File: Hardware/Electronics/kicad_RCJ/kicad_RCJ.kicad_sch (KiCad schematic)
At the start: 46 parts, among them J1 Raspberry_Pi_2_3, U23 TCS34725, U24 APDS9960

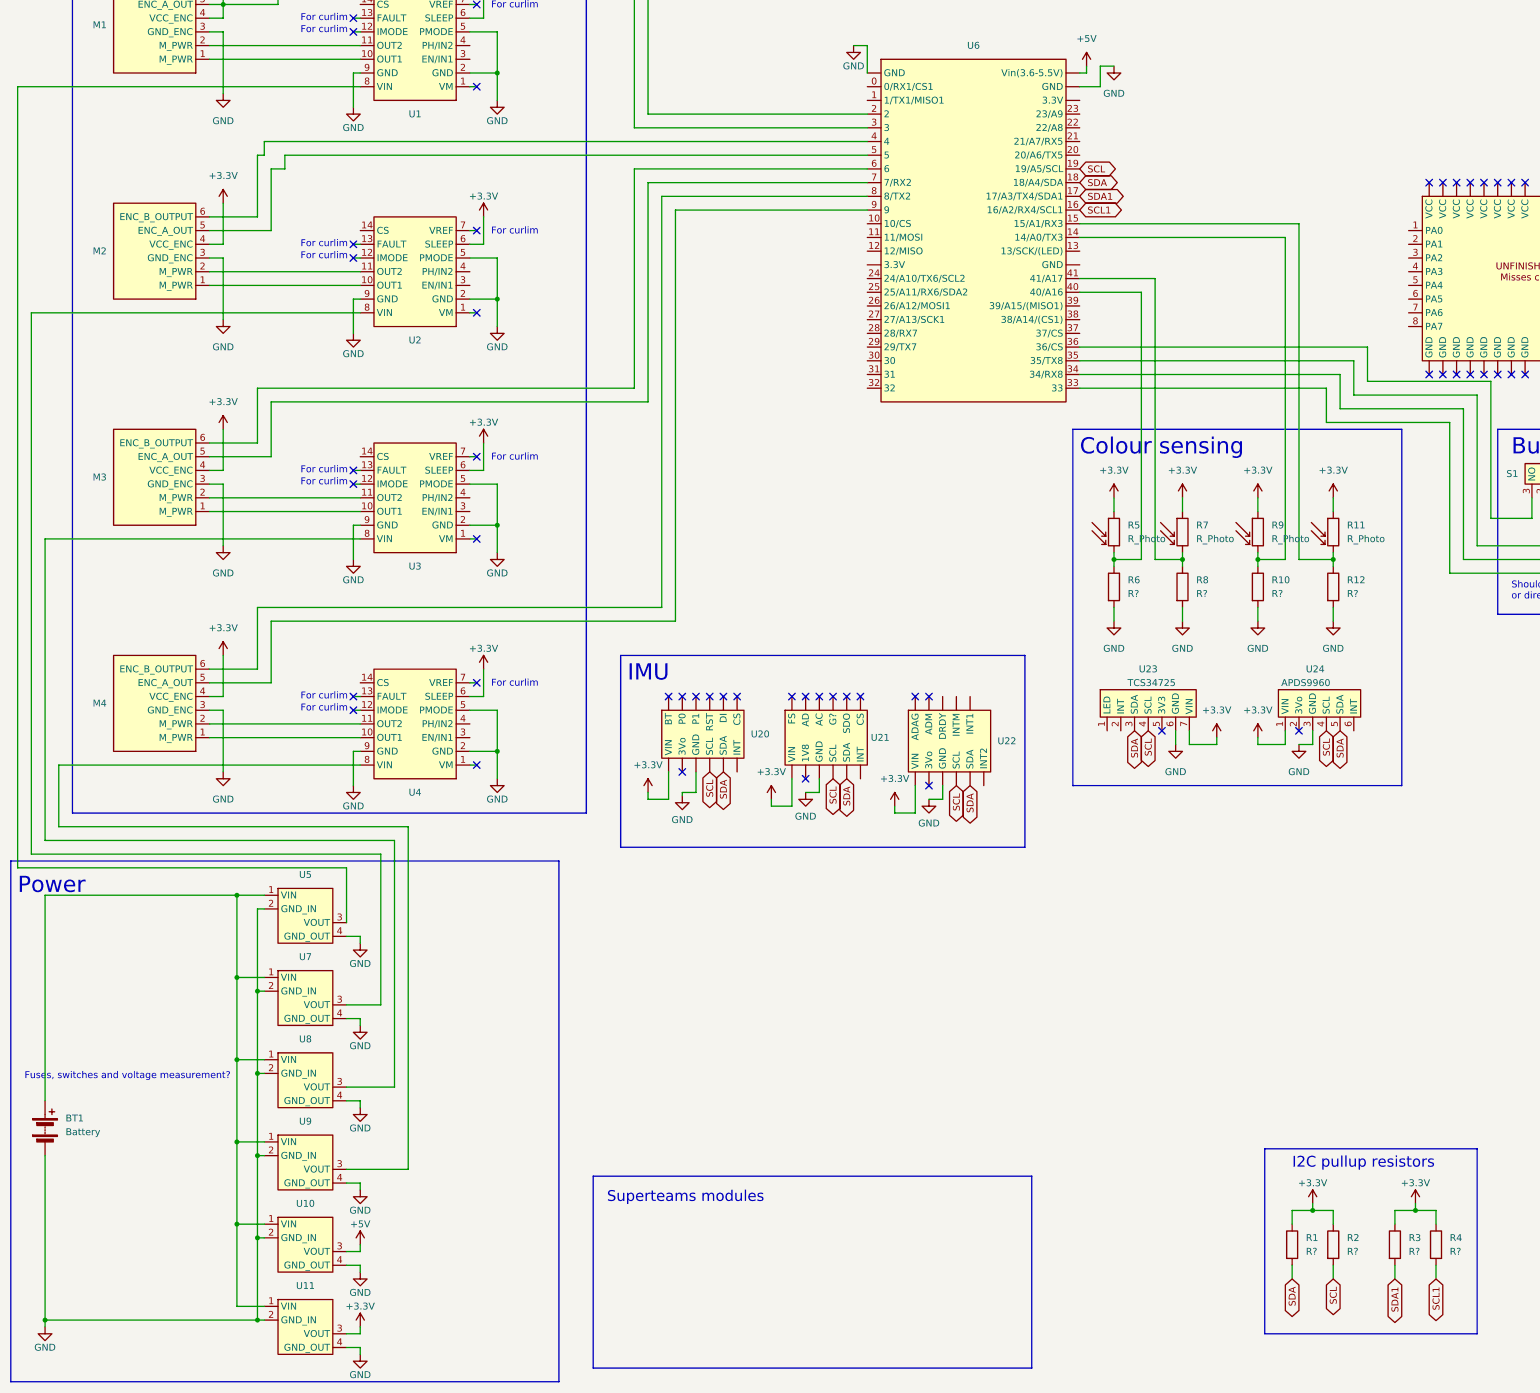
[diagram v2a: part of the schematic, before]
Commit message: added voltage divider and measurement for battery voltage
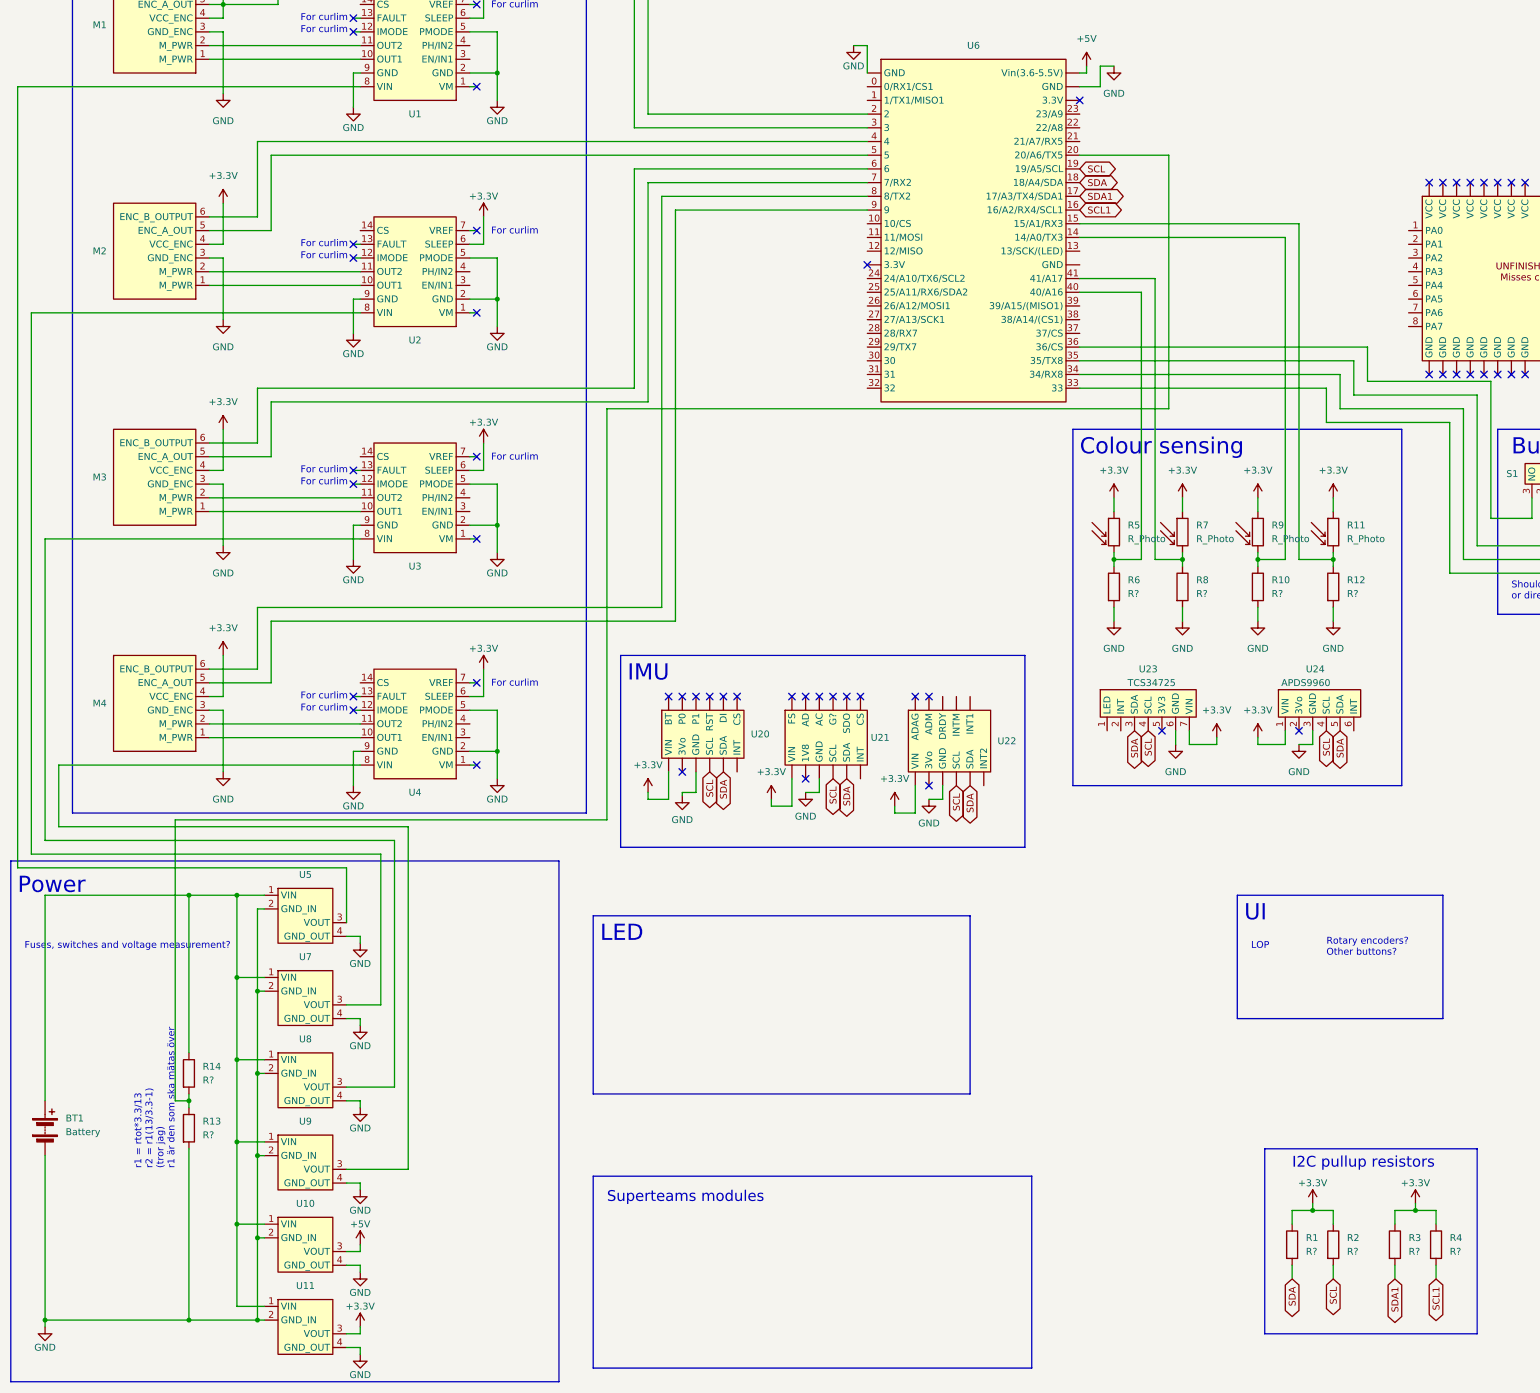
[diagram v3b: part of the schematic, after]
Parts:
- added R13, R14: R?, symbol Device:R
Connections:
- net GND: now also R13.2
- net at BT1.1 (+), U10.1 (VIN), U11.1 (VIN)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: now also R14.1
- net at U6.20 (20/A6/TX5): now also R13.1, R14.2
- no-connect marks 78 -> 80
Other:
- note added: "LED"
- note added: "LOP"
- note added: "Rotary encoders? Other buttons?"
- note added: "UI"
- note added: "r1 = rtot*3.3/13 r2 = r1(13/3.3-1) (tror jag) r1 är den som ska mätas över"
- company: (none) -> ED Robotics
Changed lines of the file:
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@@
 (kicad_sch (version 20230121) (generator eeschema)
   (paper "A3")
+  (title_block
+    (company "ED Robotics")
+  )
+  (junction (at 45.72 193.04) (diameter 0) (color 0 0 0 0)
+  )
   (junction (at 102.87 166.37) (diameter 0) (color 0 0 0 0)
   )
@@
   (junction (at 102.87 124.46) (diameter 0) (color 0 0 0 0)
   )
+  (junction (at 45.72 231.14) (diameter 0) (color 0 0 0 0)
+  )
   (junction (at 58.42 241.3) (diameter 0) (color 0 0 0 0)
   )
@@
   )
   (junction (at 243.84 130.81) (diameter 0) (color 0 0 0 0)
+  )
+  (junction (at 45.72 271.78) (diameter 0) (color 0 0 0 0)
   )
   (junction (at 254 251.46) (diameter 0) (color 0 0 0 0)
@@
   (no_connect (at 76.2 158.75))
   (no_connect (at 144.78 156.21))
+  (no_connect (at 210.82 45.72))
   (no_connect (at 387.985 62.23))
   (no_connect (at 280.67 60.96))
@@
   (no_connect (at 290.83 60.96))
   (no_connect (at 275.59 96.52))
+  (no_connect (at 171.45 76.2))
   (no_connect (at 297.18 119.38))
   (no_connect (at 285.75 60.96))
@@
   (no_connect (at 387.985 40.64))
   (no_connect (at 290.83 96.52))
-  (wire (pts (xy 60.96 58.42) (xy 60.96 69.85))
+  (wire (pts (xy 60.96 55.88) (xy 60.96 69.85))
     (stroke (width 0) (type default))
   )
@@
     (stroke (width 0) (type default))
   )
-  (wire (pts (xy 59.69 53.34) (xy 171.45 53.34))
+  (wire (pts (xy 58.42 53.34) (xy 171.45 53.34))
     (stroke (width 0) (type default))
   )
@@
     (stroke (width 0) (type default))
   )
+  (wire (pts (xy 123.19 179.07) (xy 123.19 102.87))
+    (stroke (width 0) (type default))
+  )
   (wire (pts (xy 76.2 30.48) (xy 77.47 30.48))
     (stroke (width 0) (type default))
@@
     (stroke (width 0) (type default))
   )
+  (wire (pts (xy 45.72 271.78) (xy 58.42 271.78))
+    (stroke (width 0) (type default))
+  )
   (wire (pts (xy 74.93 243.84) (xy 86.36 243.84))
     (stroke (width 0) (type default))
@@
     (stroke (width 0) (type default))
   )
-  (wire (pts (xy 59.69 55.88) (xy 59.69 53.34))
-    (stroke (width 0) (type default))
-  )
   (wire (pts (xy 358.14 45.72) (xy 354.33 45.72))
     (stroke (width 0) (type default))
@@
     (stroke (width 0) (type default))
   )
-  (wire (pts (xy 63.5 55.88) (xy 171.45 55.88))
+  (wire (pts (xy 60.96 55.88) (xy 171.45 55.88))
     (stroke (width 0) (type default))
   )
@@
     (stroke (width 0) (type default))
   )
-  (wire (pts (xy 63.5 58.42) (xy 63.5 55.88))
-    (stroke (width 0) (type default))
-  )
   (wire (pts (xy 325.12 119.38) (xy 325.12 121.92))
     (stroke (width 0) (type default))
@@
     (stroke (width 0) (type default))
   )
+  (wire (pts (xy 45.72 193.04) (xy 54.61 193.04))
+    (stroke (width 0) (type default))
+  )
   (wire (pts (xy 59.69 16.51) (xy 130.81 16.51))
     (stroke (width 0) (type default))
@@
     (stroke (width 0) (type default))
   )
+  (wire (pts (xy 227.33 55.88) (xy 210.82 55.88))
+    (stroke (width 0) (type default))
+  )
   (wire (pts (xy 322.58 82.55) (xy 377.825 82.55))
     (stroke (width 0) (type default))
@@
     (stroke (width 0) (type default))
   )
-  (wire (pts (xy 58.42 55.88) (xy 58.42 67.31))
+  (wire (pts (xy 58.42 53.34) (xy 58.42 67.31))
     (stroke (width 0) (type default))
   )
@@
     (stroke (width 0) (type default))
   )
+  (wire (pts (xy 45.72 240.03) (xy 45.72 271.78))
+    (stroke (width 0) (type default))
+  )
+  (wire (pts (xy 43.18 179.07) (xy 123.19 179.07))
+    (stroke (width 0) (type default))
+  )
   (wire (pts (xy 100.33 72.39) (xy 100.33 67.31))
     (stroke (width 0) (type default))
@@
     (stroke (width 0) (type default))
   )
-  (wire (pts (xy 19.05 193.04) (xy 54.61 193.04))
+  (wire (pts (xy 19.05 193.04) (xy 45.72 193.04))
     (stroke (width 0) (type default))
   )
@@
     (stroke (width 0) (type default))
   )
+  (wire (pts (xy 123.19 102.87) (xy 227.33 102.87))
+    (stroke (width 0) (type default))
+  )
   (wire (pts (xy 259.08 102.87) (xy 259.08 96.52))
     (stroke (width 0) (type default))
@@
     (stroke (width 0) (type default))
   )
+  (wire (pts (xy 43.18 231.14) (xy 43.18 179.07))
+    (stroke (width 0) (type default))
+  )
   (wire (pts (xy 387.985 45.72) (xy 384.175 45.72))
     (stroke (width 0) (type default))
@@
     (stroke (width 0) (type default))
   )
+  (wire (pts (xy 45.72 231.14) (xy 45.72 232.41))
+    (stroke (width 0) (type default))
+  )
   (wire (pts (xy 49.53 72.39) (xy 52.07 72.39))
     (stroke (width 0) (type default))
@@
     (stroke (width 0) (type default))
   )
+  (wire (pts (xy 227.33 102.87) (xy 227.33 55.88))
+    (stroke (width 0) (type default))
+  )
   (wire (pts (xy 243.84 139.7) (xy 243.84 142.24))
     (stroke (width 0) (type default))
@@
     (stroke (width 0) (type default))
   )
-  (wire (pts (xy 60.96 58.42) (xy 63.5 58.42))
-    (stroke (width 0) (type default))
-  )
   (wire (pts (xy 130.81 101.6) (xy 130.81 60.96))
     (stroke (width 0) (type default))
@@
     (stroke (width 0) (type default))
   )
+  (wire (pts (xy 45.72 193.04) (xy 45.72 222.25))
+    (stroke (width 0) (type default))
+  )
   (wire (pts (xy 76.2 166.37) (xy 76.2 172.72))
     (stroke (width 0) (type default))
@@
     (stroke (width 0) (type default))
   )
-  (wire (pts (xy 58.42 55.88) (xy 59.69 55.88))
-    (stroke (width 0) (type default))
-  )
   (wire (pts (xy 229.87 139.7) (xy 229.87 142.24))
     (stroke (width 0) (type default))
@@
     (stroke (width 0) (type default))
   )
-  (wire (pts (xy 19.05 271.78) (xy 58.42 271.78))
+  (wire (pts (xy 19.05 271.78) (xy 45.72 271.78))
     (stroke (width 0) (type default))
   )
@@
     (stroke (width 0) (type default))
   )
+  (wire (pts (xy 45.72 229.87) (xy 45.72 231.14))
+    (stroke (width 0) (type default))
+  )
   (wire (pts (xy 49.53 153.67) (xy 60.96 153.67))
     (stroke (width 0) (type default))
@@
     (stroke (width 0) (type default))
   )
+  (wire (pts (xy 45.72 231.14) (xy 43.18 231.14))
+    (stroke (width 0) (type default))
+  )
   (wire (pts (xy 217.17 130.81) (xy 217.17 132.08))
     (stroke (width 0) (type default))
@@
   )
   (rectangle (start 325.12 12.7) (end 405.13 104.14)
+    (stroke (width 0) (type default))
+    (fill (type none))
+  )
+  (rectangle (start 120.65 196.85) (end 190.5 229.87)
+    (stroke (width 0) (type default))
+    (fill (type none))
+  )
+  (rectangle (start 240.03 193.04) (end 278.13 215.9)
     (stroke (width 0) (type default))
     (fill (type none))
@@
   (text "For curlim" (at 110.5156 112.6947 0)
     (effects (font (size 1.27 1.27)) (justify right bottom))
+  )
+  (text "r1 = rtot*3.3/13\nr2 = r1(13/3.3-1)\n(tror jag)\nr1 är den som ska mätas över"
+    (at 43.18 243.84 90)
+    (effects (font (size 1.27 1.27)) (justify left bottom))
   )
   (text "Take 3.3V rail from RPi, from Teensy or from separate converter?"
@@
     (effects (font (size 3 3)) (justify left bottom))
   )
+  (text "LED" (at 121.92 201.93 0)
+    (effects (font (size 3 3)) (justify left bottom))
+  )
   (text "Superteams modules" (at 123.19 250.19 0)
     (effects (font (size 2 2)) (justify left bottom))
   )
-  (text "Fuses, switches and voltage measurement?" (at 15.24 227.33 0)
+  (text "Rotary encoders?\nOther buttons?" (at 256.54 204.47 0)
+    (effects (font (size 1.27 1.27)) (justify left bottom))
+  )
+  (text "Fuses, switches and voltage measurement?" (at 15.24 203.2 0)
     (effects (font (size 1.27 1.27)) (justify left bottom))
   )
@@
   (text "For curlim" (at 110.5156 154.6047 0)
     (effects (font (size 1.27 1.27)) (justify right bottom))
+  )
+  (text "LOP" (at 242.57 203.2 0)
+    (effects (font (size 1.27 1.27)) (justify left bottom))
+  )
+  (text "UI" (at 241.3 198.12 0)
+    (effects (font (size 3 3)) (justify left bottom))
   )
   (text "Bump switches" (at 290.83 111.76 0)
@@
     )
   )
+  (symbol (lib_id "Device:R") (at 45.72 226.06 0) (unit 1)
+    (in_bom yes) (on_board yes) (dnp no) (fields_autoplaced)
+    (property "Reference" "R14" (at 48.26 224.79 0)
+      (effects (font (size 1.27 1.27)) (justify left))
+    )
+    (property "Value" "R?" (at 48.26 227.33 0)
+      (effects (font (size 1.27 1.27)) (justify left))
+    )
+    (property "Footprint" "" (at 43.942 226.06 90)
+      (effects (font (size 1.27 1.27)) hide)
+    )
+    (property "Datasheet" "~" (at 45.72 226.06 0)
+      (effects (font (size 1.27 1.27)) hide)
+    )
+    (pin "1")
+    (pin "2")
+    (instances
+      (project "kicad_RCJ"
+        (path "/059f4f8e-9154-457c-9090-0b3d5df15910"
+          (reference "R14") (unit 1)
+        )
+      )
+    )
+  )
   (symbol (lib_id "power:GND") (at 229.87 142.24 0) (unit 1)
     (in_bom yes) (on_board yes) (dnp no) (fields_autoplaced)
@@
         )
       )
+    )
+  )
+  (symbol (lib_id "Device:R") (at 45.72 236.22 0) (unit 1)
+    (in_bom yes) (on_board yes) (dnp no) (fields_autoplaced)
+    (property "Reference" "R13" (at 48.26 234.95 0)
+      (effects (font (size 1.27 1.27)) (justify left))
+    )
+    (property "Value" "R?" (at 48.26 237.49 0)
+      (effects (font (size 1.27 1.27)) (justify left))
+    )
+    (property "Footprint" "" (at 43.942 236.22 90)
+      (effects (font (size 1.27 1.27)) hide)
+    )
+    (property "Datasheet" "~" (at 45.72 236.22 0)
+      (effects (font (size 1.27 1.27)) hide)
+    )
+    (pin "1")
+    (pin "2")
+    (instances
+      (project "kicad_RCJ"
+        (path "/059f4f8e-9154-457c-9090-0b3d5df15910"
+          (reference "R13") (unit 1)
+        )
+      )

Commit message: misc. electronics work
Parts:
- U20: value ~ -> BNO085
- U21: value ~ -> ICM20948
- U22: value ~ -> LSM6DSOX+LIS3MDL
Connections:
- net +3.3V: no longer M1.5 (ENC_A_OUT), U6.3
- net SCL: now also U19.18 (C/SCL)
- net SDA: now also U19.17 (D/SDA)
- net at M2.5 (ENC_A_OUT): now also U6.3; no longer U6.5
- net at M2.6 (ENC_B_OUTPUT): now also U6.2; no longer U6.4
- net at U1.3 (EN/IN1): now also U6.8 (8/TX2)
- net at U1.4 (PH/IN2): now also U6.28 (28/RX7)
- net at M1.6 (ENC_B_OUTPUT): now also U6.0 (0/RX1/CS1); no longer U6.2
- net at M4.5 (ENC_A_OUT): now also U6.7 (7/RX2); no longer U6.9
- net at M4.6 (ENC_B_OUTPUT): now also U6.6; no longer U6.8 (8/TX2)
- net at M3.5 (ENC_A_OUT): now also U6.5; no longer U6.7 (7/RX2)
- net at M3.6 (ENC_B_OUTPUT): now also U6.4; no longer U6.6
- net at U2.3 (EN/IN1): now also U6.9
- net at U2.4 (PH/IN2): now also U6.29 (29/TX7)
- net at U4.3 (EN/IN1): now also U6.11 (11/MOSI)
- net at U4.4 (PH/IN2): now also U6.31
- net at U3.3 (EN/IN1): now also U6.10 (10/CS)
- net at U3.4 (PH/IN2): now also U6.30
- net at U6.1 (1/TX1/MISO1): now also M1.5 (ENC_A_OUT)
- no-connect marks 80 -> 50
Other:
- note added: "ENCODER LOGIC LEVELS MUST BE FIXED"
- moved on the sheet: U15

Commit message: misc. electronics work
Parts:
- added D1, D2, D3, D4, D5, D6: ~, symbol RCJ_parts:small_LED
- added D7, D8: WS2812, symbol RCJ_parts:led_strip_WS2812
- added F1: Fuse, symbol Device:Fuse
- added J2: Conn_01x06, symbol Connector_Generic:Conn_01x06
- added J3, J4, J5, J6: Conn_01x02, symbol Connector_Generic:Conn_01x02
- added J7: Conn_01x01, symbol Connector_Generic:Conn_01x01
- added M5, M6: ~, symbol RCJ_parts:Servo
- added S5: ~, symbol RCJ_parts:Switch
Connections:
- net +3.3V: now also U19. (VCC), J4.1 (Pin_1)
- net +5V: now also J1.2 (5V), U6.47 (Vin(3.6-5.5V)), J5.2 (Pin_2), M5.1 (VIN), M6.1 (VIN); no longer U6. (Vin(3.6-5.5V))
- net GND: now also J1.6 (GND), U19. (VCC), U6.42 (GND), U6.46 (GND), D3.1 (GND), D4.1 (GND), D5.1 (GND), D6.1 (GND), D7.3 (GND), D8.3 (GND), J4.2 (Pin_2), J5.1 (Pin_1), M5.2 (GND), M6.2 (GND), S5.2 (COM); no longer U6. (Vin(3.6-5.5V))
- net SCL1: now also J6.2 (Pin_2)
- net SDA1: now also J6.1 (Pin_1)
- net at R14.1, U10.1 (VIN), U11.1 (VIN)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: now also F1.1; no longer BT1.1 (+)
- net at U19.8 (PA7): now also U23.1 (LED)
- net at U23.2 (INT): now also J3.2 (Pin_2)
- net at U24.6 (INT): now also J3.1 (Pin_1)
- net at U6.22 (22/A8): now also M6.3 (SIGNAL)
- net at U6.23 (23/A9): now also M5.3 (SIGNAL)
- new net: J2.3 (Pin_3), U21. (VIN)
- new net: D7.2 (SIGNAL), D8.2 (SIGNAL)
- new net: J7.1 (Pin_1), S5.1 (P1)
- new net: J2.1 (Pin_1), U22. (VIN)
- new net: J2.2 (Pin_2), U22. (VIN)
- new net: J2.5 (Pin_5), U22. (VIN)
- new net: J2.6 (Pin_6), U22. (VIN)
- new net: J2.4 (Pin_4), U20. (VIN)
- new net: BT1.1 (+), F1.2
- no-connect marks 50 -> 57
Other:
- note added: "Pi Headers"
- note added: "Rescue kit mechanism"
- moved on the sheet: J1, U12, U14, U16, U17, U18, U20, U21, U22
